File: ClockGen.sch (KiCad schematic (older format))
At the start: 0 parts

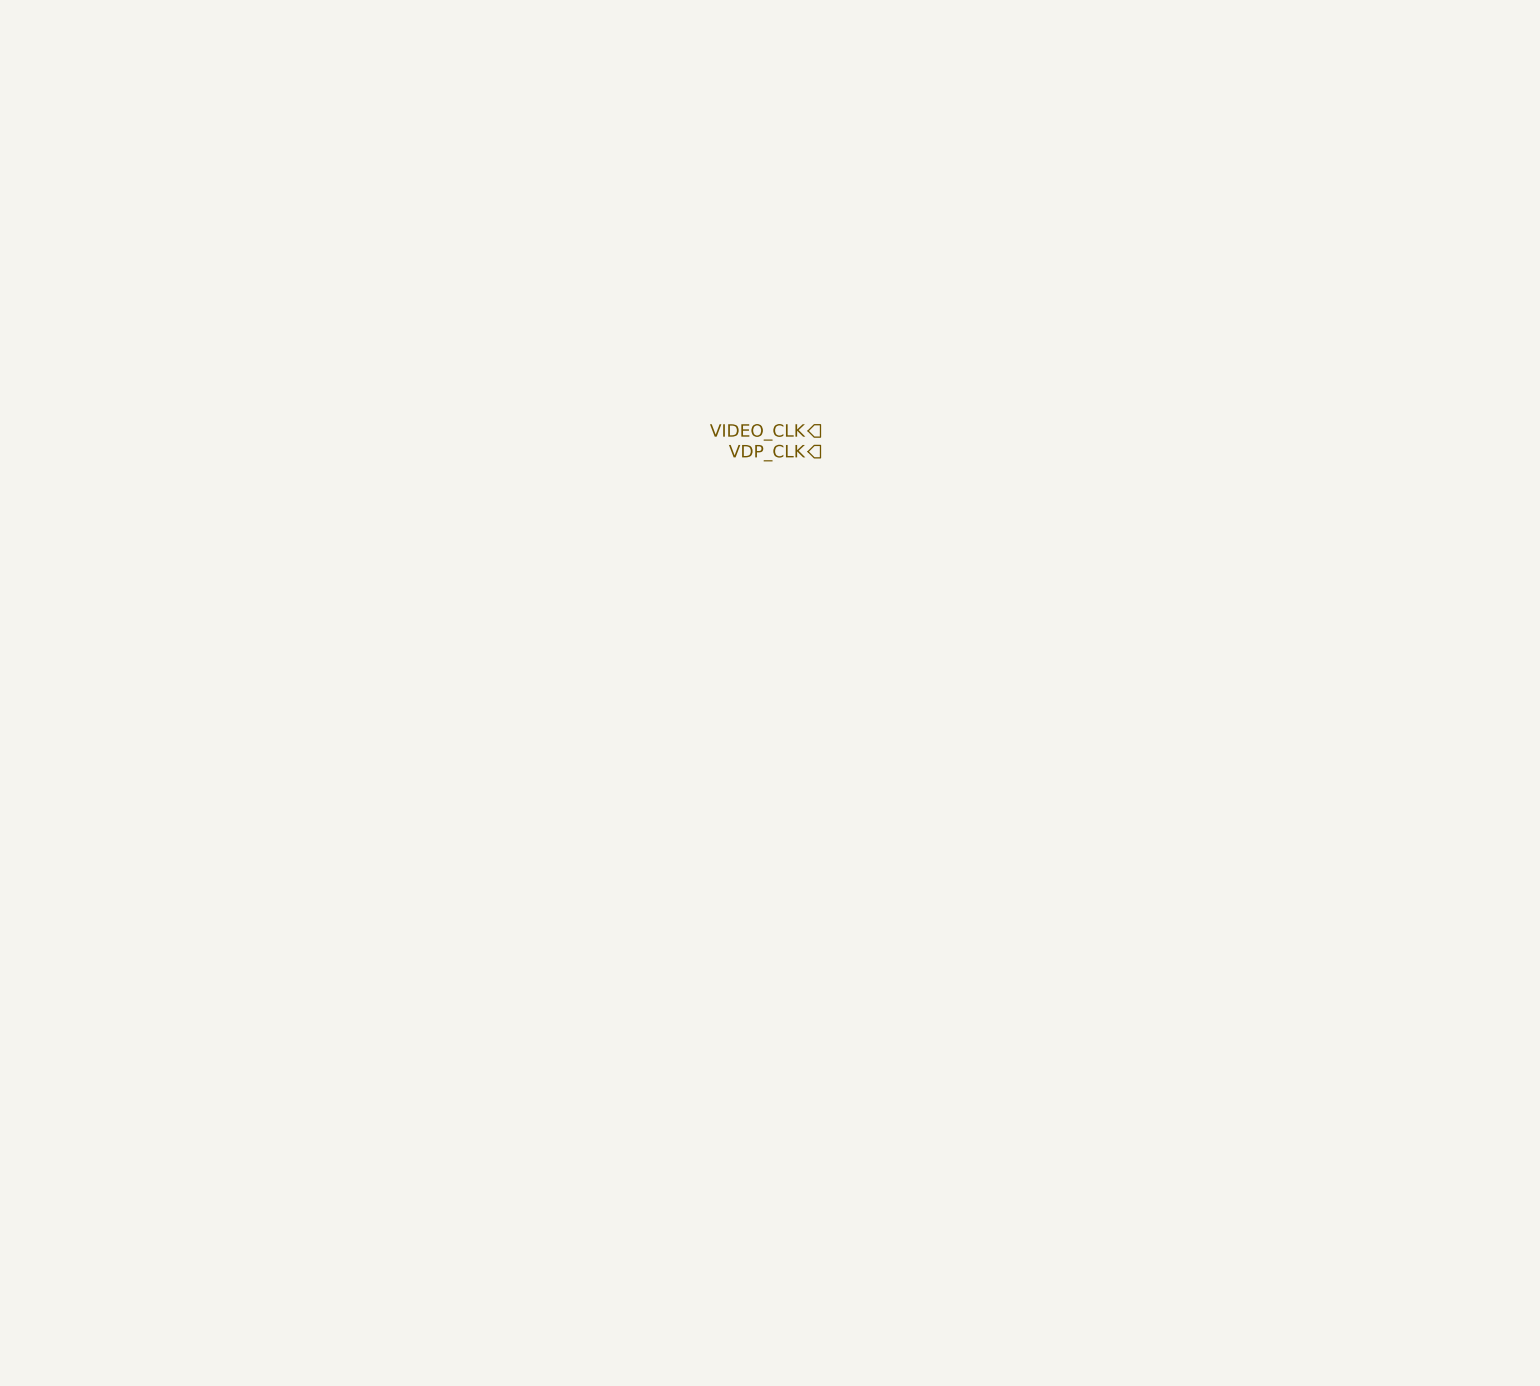
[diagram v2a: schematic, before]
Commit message: Started the clock generation schematics
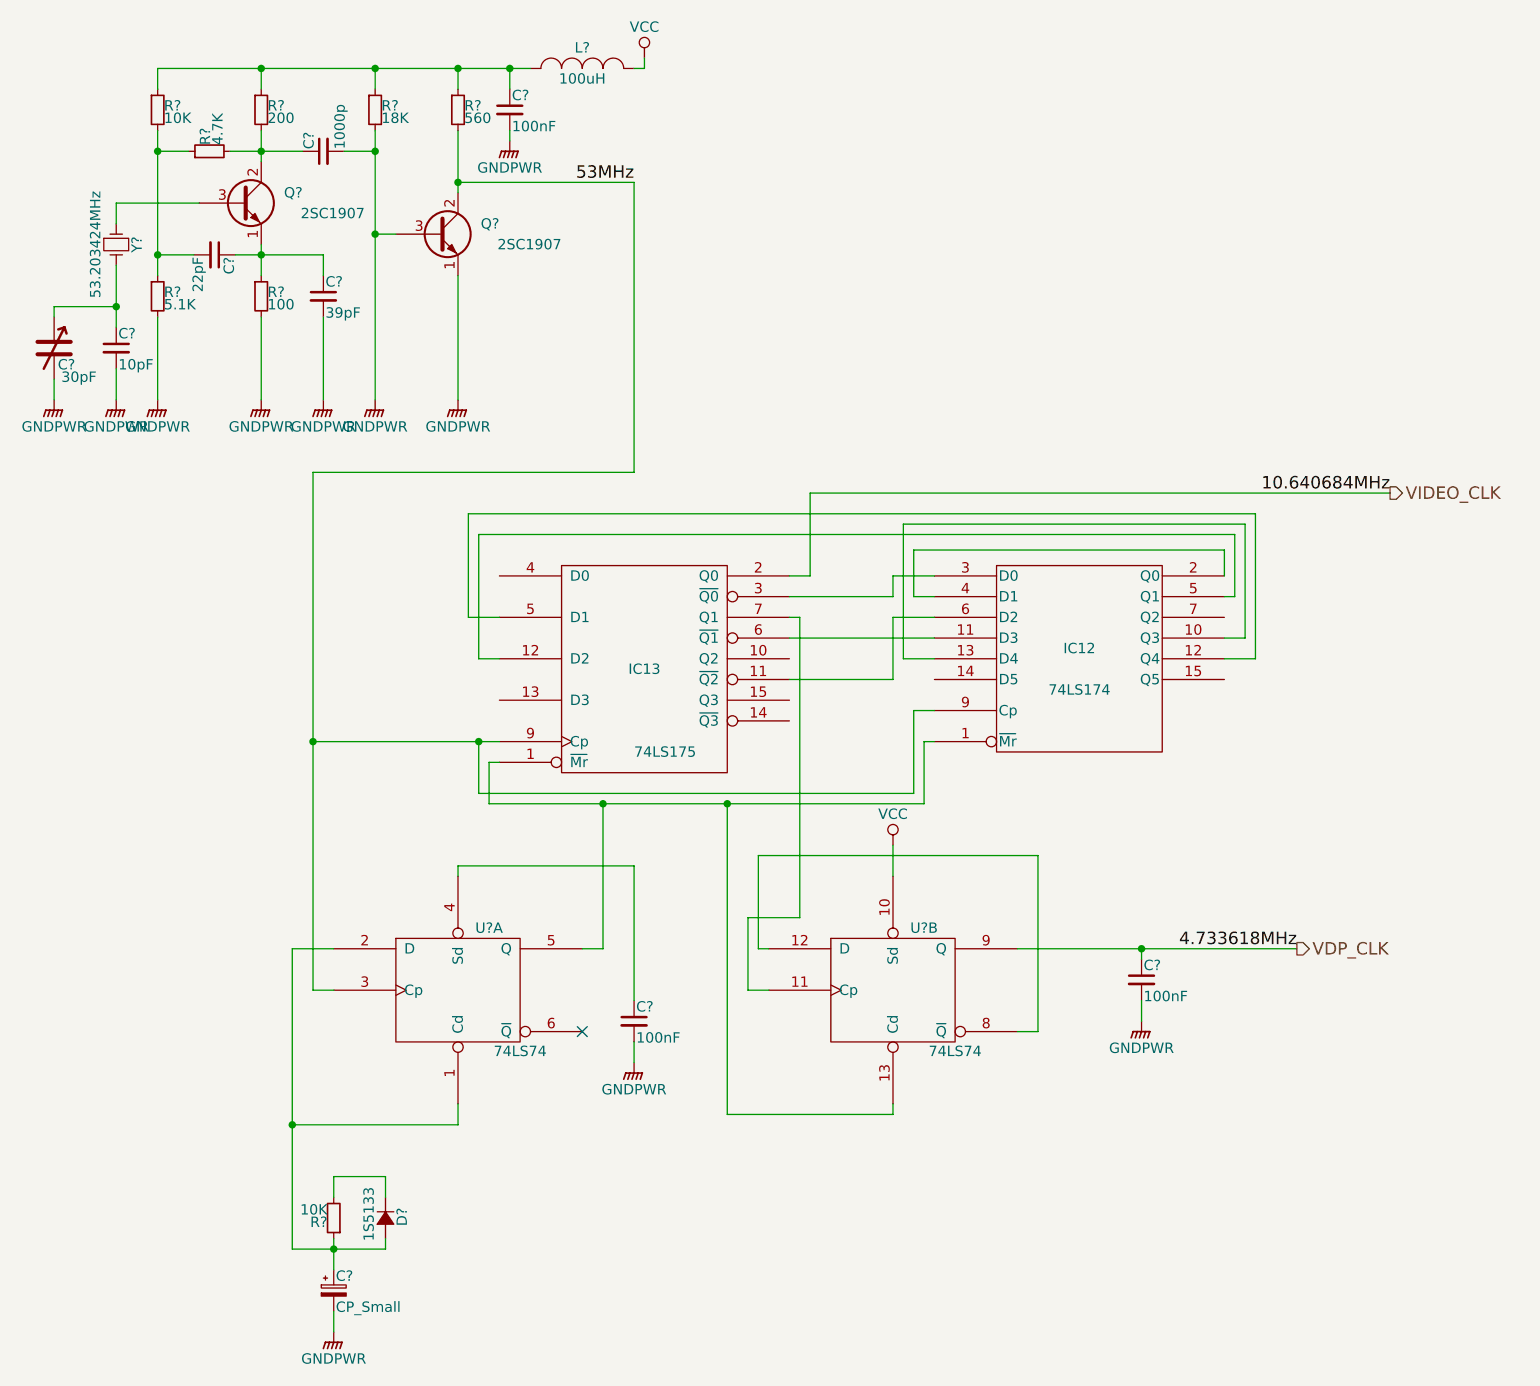
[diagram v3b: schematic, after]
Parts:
- added C?: 30pF, symbol CTRIM
- added C?: 10pF, symbol C_Small
- added C?: 22pF, symbol C_Small
- added C?: 39pF, symbol C_Small
- added C?: 1000p, symbol C_Small
- added C? (x3): 100nF, symbol C_Small
- added C?: CP_Small, symbol CP_Small
- added D?: 1S5133, symbol D_Small
- added IC12: 74LS174, symbol 74LS174
- added IC13: 74LS175, symbol 74LS175
- added L?: 100uH, symbol INDUCTOR_SMALL
- added Q? (x2): 2SC1907, symbol Q_NPN_ECB
- added R? (x2): 10K, symbol R_Small
- added R?: 5.1K, symbol R_Small
- added R?: 100, symbol R_Small
- added R?: 4.7K, symbol R_Small
- added R?: 200, symbol R_Small
- added R?: 18K, symbol R_Small
- added R?: 560, symbol R_Small
- added U? (x2): 74LS74, symbol 74LS74
- added Y?: 53.203424MHz, symbol Crystal_Small
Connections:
- net VDP_CLK: now also C?.1, U?.9 (Q)
- net VIDEO_CLK: now also IC13.2 (Q0)
- new net: IC12.1 (~Mr), IC13.1 (~Mr), U?.13 (Cd), U?.5 (Q)
- new net: IC12.10 (Q3), IC12.13 (D4)
- new net: IC12.11 (D3), IC13.6 (~Q1)
- new net: IC12.12 (Q4), IC13.5 (D1)
- new net: IC12.2 (Q0), IC12.4 (D1)
- new net: IC12.3 (D0), IC13.3 (~Q0)
- new net: IC12.5 (Q1), IC13.12 (D2)
- new net: IC12.6 (D2), IC13.11 (~Q2)
- new net: IC13.7 (Q1), U?.11 (Cp)
- new net: C?.1, C?.1, Y?.2
- new net: Q?.3 (B), Y?.1
- new net: C?.1, C?.1, Q?.1 (E), R?.1
- new net: C?.1, Q?.2 (C), R?.2, R?.2
- new net: C?.1, L?.1, R?.1, R?.1, R?.1, R?.1
- new net: C?.2, R?.1, R?.1, R?.2
- new net: C?.1, D?.2 (A), R?.1, U?.1 (Cd), U?.2 (D)
- new net: C?.1, U?.4 (Sd)
- new net: U?.12 (D), U?.8 (~Q)
- new net: D?.1 (K), R?.2
- new net 53MHz: IC12.9 (Cp), IC13.9 (Cp), Q?.2 (C), R?.2, U?.3 (Cp)
- new net GND: IC12.8 (GND), IC13.8 (GND), U?.7 (GND), U?.7 (GND)
- new net GNDPWR: C?.2, C?.2, C?.2, C?.2, C?.2, C?.2, C?.2, C?.2, Q?.1 (E), Q?.3 (B), R?.2, R?.2, R?.2
- new net VCC: IC12.16 (VCC), IC13.16 (VCC), L?.2, U?.10 (Sd), U?.14 (VCC), U?.14 (VCC)
- no-connect marks 0 -> 1
